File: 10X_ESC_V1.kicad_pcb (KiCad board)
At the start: 4 copper layers, 99.8 x 61.8 mm, 70 parts, among them J1 Conn_01x05_MountingPin, Q1 BUK7Y1R4-40H, Q2 BUK7Y1R4-40H, Q3 BUK7Y1R4-40H, Q4 BUK7Y1R4-40H, Q5 BUK7Y1R4-40H, Q7 BUK7Y1R4-40H, U1 STM32F051K8Ux, U2 DRV8300DPWR, U3 TPS70933DBVR, U4 TPS62932

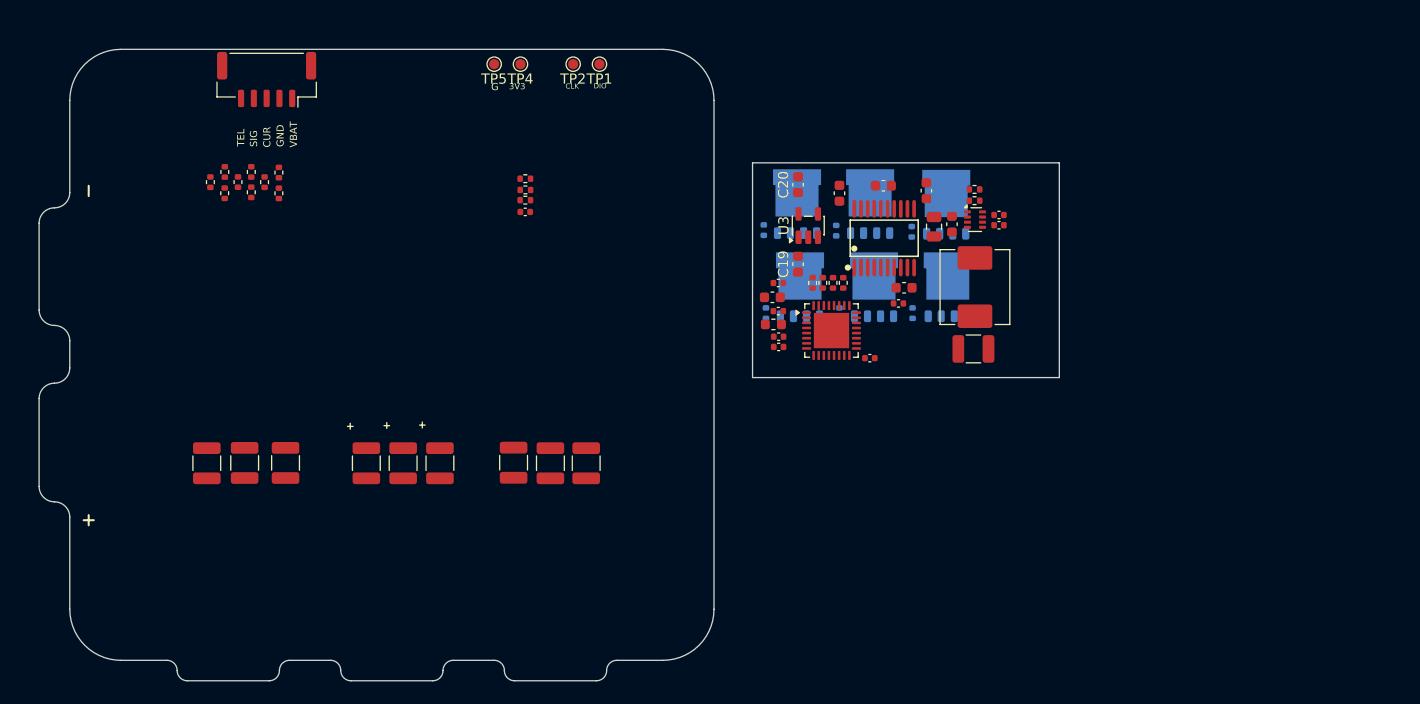
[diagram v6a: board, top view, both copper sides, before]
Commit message: V2 배치 완료: 36x21 양면, 납땜 패드 배치
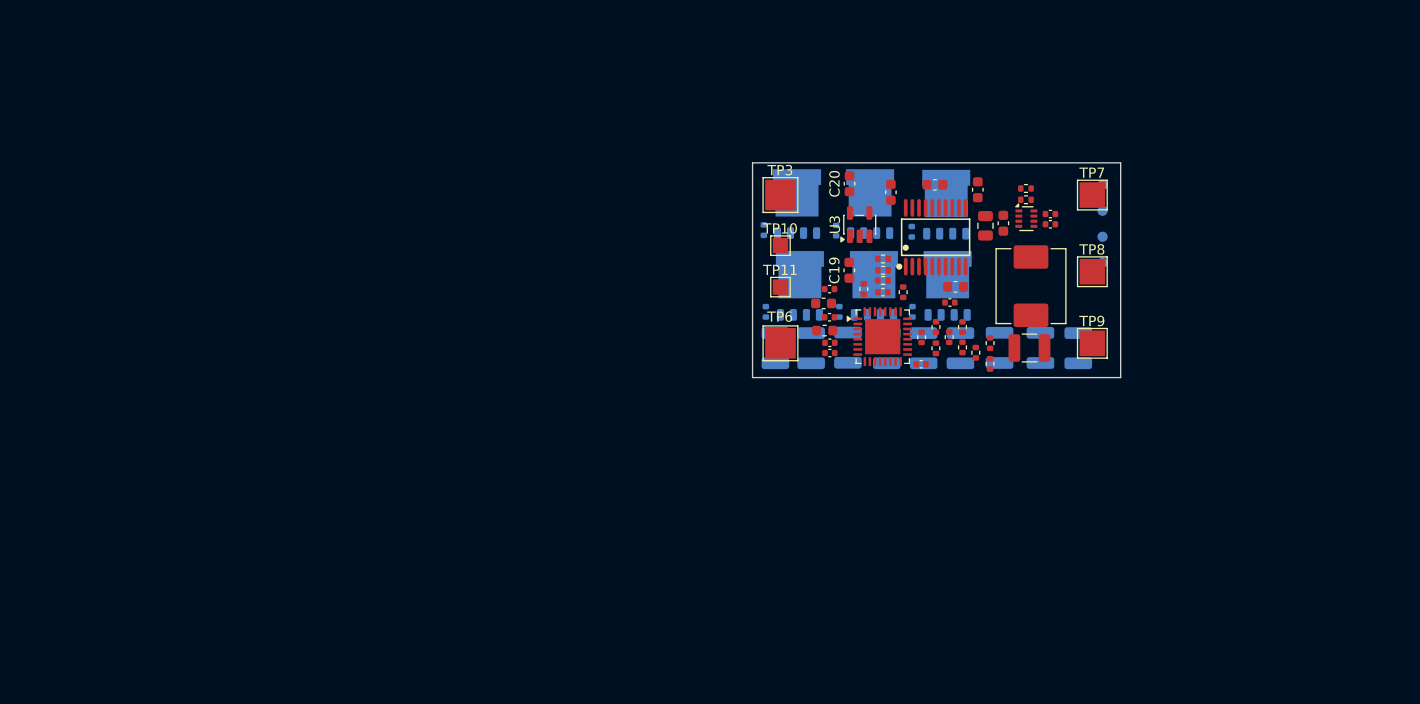
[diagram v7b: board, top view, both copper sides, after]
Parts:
- removed G***: LOGO, LOGO
- removed J1: Conn_01x05_MountingPin, Connector_JST:JST_GH_SM05B-GHS-TB_1x05-1MP_P1.25mm_Horizontal
- removed R28, R29: 33, Resistor_SMD:R_0402_1005Metric
- added TP10: SIGNAL_INPUT, TestPoint:TestPoint_Pad_1.5x1.5mm, F.Cu at (152.5, 96.5)
- added TP11: GND, TestPoint:TestPoint_Pad_1.5x1.5mm, F.Cu at (152.5, 100.5)
- added TP3: +BATT, TestPoint:TestPoint_Pad_3.0x3.0mm, F.Cu at (152.5, 91.5)
- added TP6: GND, TestPoint:TestPoint_Pad_3.0x3.0mm, F.Cu at (152.5, 106.0)
- added TP7: MOTORA, TestPoint:TestPoint_Pad_2.5x2.5mm, F.Cu at (183.0, 91.5)
- added TP8: MOTORB, TestPoint:TestPoint_Pad_2.5x2.5mm, F.Cu at (183.0, 99.0)
- added TP9: MOTORC, TestPoint:TestPoint_Pad_2.5x2.5mm, F.Cu at (183.0, 106.0)
- C10, C11, C12, C13, C33, C34, C7, C8, C9, TP1, TP2, TP4, TP5: moved to B.Cu
- moved C8 86.0 mm to (181.6, 106.5)
- moved C13 78.6 mm to (177.9, 106.5)
- moved R15 71.5 mm to (173.0, 106.0)
- moved R18 71.5 mm to (173.0, 108.0)
- moved R21 71.5 mm to (171.6, 106.9)
- moved R16 71.2 mm to (170.3, 104.4)
- moved R17 71.2 mm to (167.7, 104.4)
- moved R19 71.2 mm to (170.3, 106.4)
- moved R23 71.2 mm to (166.3, 105.4)
- moved R22 71.2 mm to (169.0, 105.4)
- moved R20 71.2 mm to (167.7, 106.5)
- moved C7 70.7 mm to (173.9, 106.5)
- moved TP5 62.6 mm to (184.0, 98.1)
- moved TP4 59.4 mm to (184.0, 95.6)
- moved C33 59.2 mm to (170.1, 106.5)
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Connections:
- U1 pad 29: Net-(U1-PB6) -> unconnected-(U1-PB6-Pad29)
- U1 pad 30: Net-(U1-PB7) -> unconnected-(U1-PB7-Pad30)
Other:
- board size 99.8 x 61.8 mm -> 36 x 21 mm
- board text removed: "3V3"
- board text removed: "6S V1 Rev1"
- board text removed: "CLK"
- board text removed: "CUR"
- board text removed: "DIO"
- board text removed: "G"
- board text removed: "GND"
- board text removed: "Motor Driver Dev Board"
- board text removed: "SIG"
- board text removed: "TEL"
- board text removed: "VBAT"

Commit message: 배선 준비: 설계 규칙, 넷 클래스 설정 및 내층 GND/+BATT 면 추가
Power/HighCurrent 넷 클래스 추가, In1=GND, In2=+BATT 구리 영역
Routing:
- added copper zone on In2.Cu, net +BATT
- added copper zone on In1.Cu, net GND
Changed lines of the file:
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@@
 		(capping no)
 		(filling no)
+		(zone_defaults)
 		(pcbplotparams
 			(layerselection 0x00000000_00000000_55555555_5755f5ff)
@@
 		(layer "Edge.Cuts")
 	)
+	(zone
+		(net "GND")
+		(layer "In1.Cu")
+		(hatch edge 0.5)
+		(connect_pads
+			(clearance 0.5)
+		)
+		(min_thickness 0.25)
+		(fill yes
+			(thermal_gap 0.5)
+			(thermal_bridge_width 0.5)
+			(island_removal_mode 0)
+		)
+		(polygon
+			(pts
+				(xy 149.5 88) (xy 149.5 110) (xy 186.5 110) (xy 186 88)
+			)
+		)
+	)
+	(zone
+		(net "+BATT")
+		(layer "In2.Cu")
+		(hatch edge 0.5)
+		(priority 1)
+		(connect_pads
+			(clearance 0.5)
+		)
+		(min_thickness 0.25)
+		(fill yes
+			(thermal_gap 0.5)
+			(thermal_bridge_width 0.5)
+			(island_removal_mode 0)
+		)
+		(polygon
+			(pts
+				(xy 186 88) (xy 149.5 88) (xy 149.5 110) (xy 186.5 110)
+			)
+		)
+	)
 	(embedded_fonts no)
